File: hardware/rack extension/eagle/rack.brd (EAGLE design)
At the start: 160 x 100 mm, 48 parts, among them IC1 74HC139N, IC2 74HC574N, IC3 74HC32N, IC4 74HC86N, IC5 74HC04N, IC6 74HC14N, IC7 74HC541N, K1 APF30212C, K2 APF30212C, Q1 BC547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

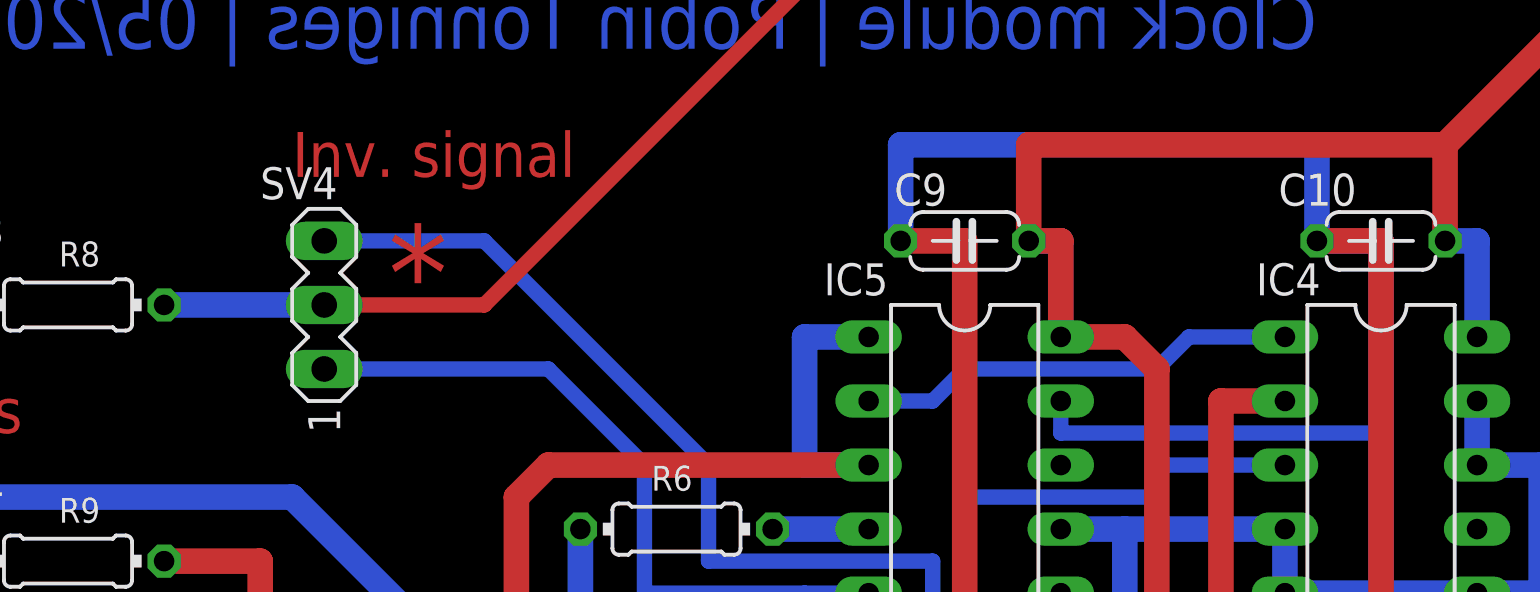
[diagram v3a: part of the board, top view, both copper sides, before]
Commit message: Value of PullUp from1k to 15k
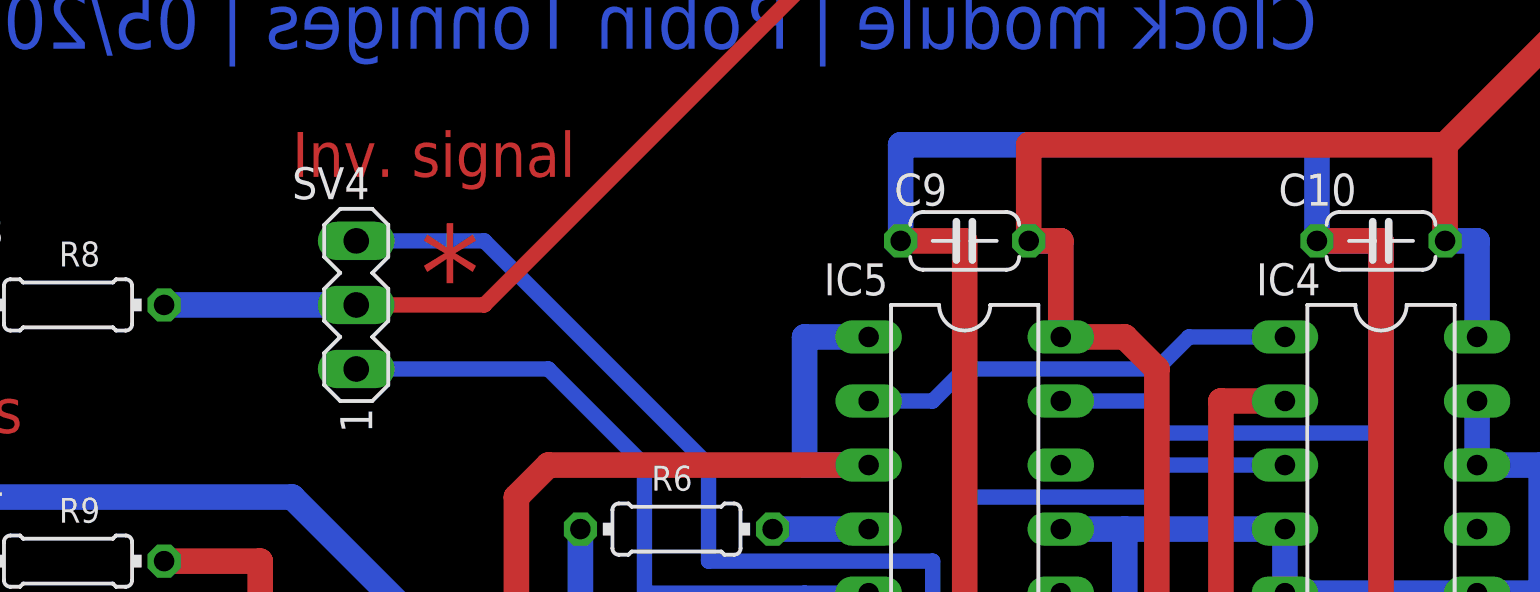
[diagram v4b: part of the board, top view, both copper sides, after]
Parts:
- R7: value 1k -> 15k
- moved SV4 1.27 mm to (30.5, 82.5)
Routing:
- net N$30: track 38.0 -> 36.7 mm
- net N$26: track 60.0 -> 58.7 mm
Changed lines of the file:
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@@
 <circle x="151.13" y="93.98" radius="2.00804375" width="1.27" layer="17"/>
 <text x="32.385" y="62.865" size="3.81" layer="1">*</text>
-<text x="31.75" y="81.915" size="3.81" layer="1">*</text>
+<text x="33.02" y="81.915" size="3.81" layer="1">*</text>
 <text x="103.505" y="13.335" size="3.81" layer="1">*</text>
 <text x="127.635" y="13.335" size="3.81" layer="1">*</text>
@@
 <attribute name="VALUE" x="27.559" y="67.31" size="1.27" layer="27" ratio="10" rot="R270"/>
 </element>
-<element name="R7" library="rcl" package="0204/7" value="1k" x="20.32" y="63.5" smashed="yes">
+<element name="R7" library="rcl" package="0204/7" value="15k" x="20.32" y="63.5" smashed="yes">
 <attribute name="NAME" x="17.78" y="64.7954" size="0.9906" layer="25" ratio="10"/>
 <attribute name="VALUE" x="18.6944" y="63.0174" size="0.9906" layer="27" ratio="10"/>
@@
 <attribute name="NAME" x="81.2438" y="1.3462" size="1.27" layer="25" ratio="10"/>
 </element>
-<element name="SV4" library="con-lstb" package="MA03-1" value="" x="29.21" y="82.55" smashed="yes" rot="R90">
-<attribute name="OC_NEWARK" value="unknown" x="29.21" y="82.55" size="1.778" layer="27" rot="R90" display="off"/>
-<attribute name="MPN" value="" x="29.21" y="82.55" size="1.778" layer="27" rot="R90" display="off"/>
-<attribute name="MF" value="" x="29.21" y="82.55" size="1.778" layer="27" rot="R90" display="off"/>
-<attribute name="OC_FARNELL" value="unknown" x="29.21" y="82.55" size="1.778" layer="27" rot="R90" display="off"/>
-<attribute name="NAME" x="26.67" y="86.741" size="1.27" layer="25" ratio="10"/>
-<attribute name="VALUE" x="32.131" y="78.74" size="1.27" layer="27" ratio="10" rot="R90"/>
+<element name="SV4" library="con-lstb" package="MA03-1" value="" x="30.48" y="82.55" smashed="yes" rot="R90">
+<attribute name="OC_NEWARK" value="unknown" x="30.48" y="82.55" size="1.778" layer="27" rot="R90" display="off"/>
+<attribute name="MPN" value="" x="30.48" y="82.55" size="1.778" layer="27" rot="R90" display="off"/>
+<attribute name="MF" value="" x="30.48" y="82.55" size="1.778" layer="27" rot="R90" display="off"/>
+<attribute name="OC_FARNELL" value="unknown" x="30.48" y="82.55" size="1.778" layer="27" rot="R90" display="off"/>
+<attribute name="NAME" x="27.94" y="86.741" size="1.27" layer="25" ratio="10"/>
+<attribute name="VALUE" x="33.401" y="78.74" size="1.27" layer="27" ratio="10" rot="R90"/>
 </element>
 <element name="IC7" library="74xx-eu" package="DIL20" value="74HC541N" x="96.52" y="77.47" smashed="yes" rot="R270">
@@
 <wire x1="77.47" y1="76.2" x2="74.93" y2="76.2" width="1.016" layer="16"/>
 <wire x1="74.93" y1="76.2" x2="74.93" y2="78.74" width="1.016" layer="16"/>
-<wire x1="58.42" y1="77.47" x2="71.12" y2="77.47" width="0.6096" layer="16"/>
+<wire x1="62.23" y1="77.47" x2="71.12" y2="77.47" width="0.6096" layer="16"/>
 <contactref element="IC7" pad="10"/>
 <contactref element="C12" pad="2"/>
@@
 <wire x1="71.12" y1="71.12" x2="67.31" y2="71.12" width="1.016" layer="16"/>
 <wire x1="71.12" y1="71.12" x2="74.93" y2="71.12" width="1.016" layer="16"/>
-<wire x1="58.42" y1="77.47" x2="58.42" y2="78.74" width="0.6096" layer="16"/>
 <wire x1="93.98" y1="92.71" x2="93.98" y2="94.615" width="1.016" layer="16"/>
 <wire x1="93.98" y1="94.615" x2="111.76" y2="94.615" width="1.016" layer="16"/>
@@
 <wire x1="52.07" y1="88.9" x2="68.58" y2="88.9" width="1.016" layer="16"/>
 <wire x1="68.58" y1="88.9" x2="68.58" y2="85.09" width="1.016" layer="16"/>
+<wire x1="62.23" y1="77.47" x2="62.23" y2="78.74" width="0.6096" layer="16"/>
+<wire x1="62.23" y1="78.74" x2="58.42" y2="78.74" width="0.6096" layer="16"/>
 </signal>
 <signal name="VCC">
@@
 <contactref element="R8" pad="1"/>
 <contactref element="SV4" pad="2"/>
-<wire x1="22.86" y1="82.55" x2="29.21" y2="82.55" width="1.016" layer="16"/>
-<wire x1="29.21" y1="82.55" x2="35.56" y2="82.55" width="0.6096" layer="1"/>
+<wire x1="22.86" y1="82.55" x2="30.48" y2="82.55" width="1.016" layer="16"/>
+<wire x1="30.48" y1="82.55" x2="35.56" y2="82.55" width="0.6096" layer="1"/>
 <wire x1="35.56" y1="82.55" x2="49.53" y2="96.52" width="0.6096" layer="1"/>
 <wire x1="152.4" y1="26.035" x2="154.94" y2="26.035" width="0.6096" layer="1"/>
@@
 <wire x1="48.26" y1="71.12" x2="41.91" y2="71.12" width="0.6096" layer="16"/>
 <wire x1="41.91" y1="71.12" x2="41.91" y2="76.2" width="0.6096" layer="16"/>
-<wire x1="38.1" y1="80.01" x2="29.21" y2="80.01" width="0.6096" layer="16"/>
+<wire x1="38.1" y1="80.01" x2="30.48" y2="80.01" width="0.6096" layer="16"/>
 <wire x1="67.31" y1="76.2" x2="62.23" y2="76.2" width="0.6096" layer="16"/>
 <wire x1="62.23" y1="76.2" x2="62.23" y2="74.93" width="0.6096" layer="16"/>
@@
 <wire x1="53.34" y1="72.39" x2="44.45" y2="72.39" width="0.6096" layer="16"/>
 <wire x1="44.45" y1="72.39" x2="44.45" y2="76.2" width="0.6096" layer="16"/>
-<wire x1="35.56" y1="85.09" x2="29.21" y2="85.09" width="0.6096" layer="16"/>
+<wire x1="35.56" y1="85.09" x2="30.48" y2="85.09" width="0.6096" layer="16"/>
 <wire x1="44.45" y1="76.2" x2="35.56" y2="85.09" width="0.6096" layer="16"/>
 </signal>

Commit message: Little layout update
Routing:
- net N$34: track 78.4 -> 81.7 mm
- net N$36: track 107.7 -> 106.8 mm
- net GND: track 771.6 -> 772.2 mm
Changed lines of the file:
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@@
 <wire x1="118.11" y1="50.8" x2="114.3" y2="50.8" width="1.016" layer="1"/>
 <wire x1="114.3" y1="50.8" x2="114.3" y2="57.15" width="1.016" layer="1"/>
-<wire x1="69.85" y1="33.02" x2="78.74" y2="33.02" width="1.016" layer="1"/>
-<wire x1="78.74" y1="33.02" x2="111.76" y2="33.02" width="1.016" layer="1"/>
+<wire x1="69.85" y1="33.02" x2="78.105" y2="33.02" width="1.016" layer="1"/>
+<wire x1="78.105" y1="33.02" x2="111.76" y2="33.02" width="1.016" layer="1"/>
 <wire x1="111.76" y1="33.02" x2="111.76" y2="30.48" width="1.016" layer="1"/>
 <wire x1="149.86" y1="10.795" x2="154.94" y2="10.795" width="1.016" layer="16"/>
@@
 <wire x1="20.32" y1="66.04" x2="17.78" y2="68.58" width="1.016" layer="16"/>
 <contactref element="S1" pad="4"/>
-<wire x1="82.55" y1="16.51" x2="78.74" y2="16.51" width="1.016" layer="16"/>
-<via x="78.74" y="16.51" extent="1-16" drill="0.6" diameter="1.4224"/>
-<wire x1="78.74" y1="16.51" x2="78.74" y2="33.02" width="1.016" layer="1"/>
+<wire x1="82.55" y1="16.51" x2="78.105" y2="16.51" width="1.016" layer="16"/>
+<via x="78.105" y="16.51" extent="1-16" drill="0.6" diameter="1.4224"/>
+<wire x1="78.105" y1="16.51" x2="78.105" y2="33.02" width="1.016" layer="1"/>
 <wire x1="50.8" y1="66.04" x2="54.61" y2="66.04" width="1.016" layer="1"/>
 <wire x1="54.61" y1="66.04" x2="54.61" y2="85.09" width="1.016" layer="1"/>
@@
 <wire x1="44.47" y1="13.97" x2="44.47" y2="10.16" width="1.016" layer="16"/>
 <wire x1="44.47" y1="10.16" x2="49.55" y2="5.08" width="1.016" layer="16"/>
-<wire x1="69.85" y1="5.08" x2="76.835" y2="12.065" width="1.016" layer="16"/>
-<wire x1="76.835" y1="12.065" x2="76.835" y2="18.415" width="1.016" layer="16"/>
-<wire x1="76.835" y1="18.415" x2="77.47" y2="19.05" width="1.016" layer="16"/>
+<wire x1="69.85" y1="5.08" x2="76.2" y2="11.43" width="1.016" layer="16"/>
+<wire x1="76.2" y1="11.43" x2="76.2" y2="17.78" width="1.016" layer="16"/>
+<wire x1="76.2" y1="17.78" x2="77.47" y2="19.05" width="1.016" layer="16"/>
 <wire x1="77.47" y1="19.05" x2="82.55" y2="19.05" width="1.016" layer="16"/>
 </signal>
@@
 <wire x1="44.45" y1="6.35" x2="47.625" y2="3.175" width="1.016" layer="16"/>
 <wire x1="47.625" y1="3.175" x2="71.12" y2="3.175" width="1.016" layer="16"/>
-<wire x1="87.63" y1="19.05" x2="91.44" y2="19.05" width="1.016" layer="16"/>
-<via x="91.44" y="19.05" extent="1-16" drill="0.6" diameter="1.4224"/>
-<wire x1="91.44" y1="19.05" x2="91.44" y2="11.43" width="1.016" layer="1"/>
-<wire x1="91.44" y1="11.43" x2="80.01" y2="11.43" width="1.016" layer="1"/>
-<via x="80.01" y="11.43" extent="1-16" drill="0.6" diameter="1.4224"/>
-<wire x1="80.01" y1="11.43" x2="79.375" y2="11.43" width="1.016" layer="16"/>
-<wire x1="79.375" y1="11.43" x2="71.12" y2="3.175" width="1.016" layer="16"/>
+<wire x1="87.63" y1="19.05" x2="92.71" y2="19.05" width="1.016" layer="16"/>
+<via x="92.71" y="19.05" extent="1-16" drill="0.6" diameter="1.4224"/>
+<wire x1="92.71" y1="19.05" x2="92.71" y2="10.16" width="1.016" layer="1"/>
+<wire x1="92.71" y1="10.16" x2="78.105" y2="10.16" width="1.016" layer="1"/>
+<via x="78.105" y="10.16" extent="1-16" drill="0.6" diameter="1.4224"/>
+<wire x1="78.105" y1="10.16" x2="71.12" y2="3.175" width="1.016" layer="16"/>
 </signal>
 <signal name="N$30">
@@
 <wire x1="107.95" y1="50.8" x2="110.49" y2="50.8" width="1.016" layer="16"/>
 <wire x1="110.49" y1="43.18" x2="107.95" y2="43.18" width="1.016" layer="16"/>
-<wire x1="93.98" y1="29.21" x2="93.98" y2="6.35" width="1.016" layer="16"/>
-<wire x1="93.98" y1="6.35" x2="129.54" y2="6.35" width="1.016" layer="16"/>
+<wire x1="94.615" y1="29.845" x2="94.615" y2="6.35" width="1.016" layer="16"/>
+<wire x1="94.615" y1="6.35" x2="129.54" y2="6.35" width="1.016" layer="16"/>
 <wire x1="133.35" y1="10.16" x2="133.35" y2="13.97" width="1.016" layer="16"/>
-<wire x1="107.95" y1="43.18" x2="93.98" y2="29.21" width="1.016" layer="16"/>
+<wire x1="107.95" y1="43.18" x2="94.615" y2="29.845" width="1.016" layer="16"/>
 <wire x1="129.54" y1="6.35" x2="133.35" y2="10.16" width="1.016" layer="16"/>
 <contactref element="SV5" pad="2"/>
